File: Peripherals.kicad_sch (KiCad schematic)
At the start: 32 parts, among them J1 1X02PICOBLADE, J3 1X02JST_SH, Q5 DMN3023L, U22 SPI_QUAD_FLASH, U4 ACCEL_LIS3DHTR, U5 PAM8301, X1 MicroSD

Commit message: Use kicad footprints for resistors/capacitors
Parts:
- C10, C14, C20: footprint 32blit:C0402K -> Capacitor_SMD:C_0402_1005Metric
- C17, C3: footprint 32blit:C0603 -> Capacitor_SMD:C_0603_1608Metric
- C23: footprint 32blit:0402 -> Capacitor_SMD:C_0402_1005Metric
- C36: footprint 32blit:C0805 -> Capacitor_SMD:C_0805_2012Metric
- R12, R17, R18, R19, R20, R24, R26, R38, R5: footprint 32blit:R0603 -> Resistor_SMD:R_0603_1608Metric

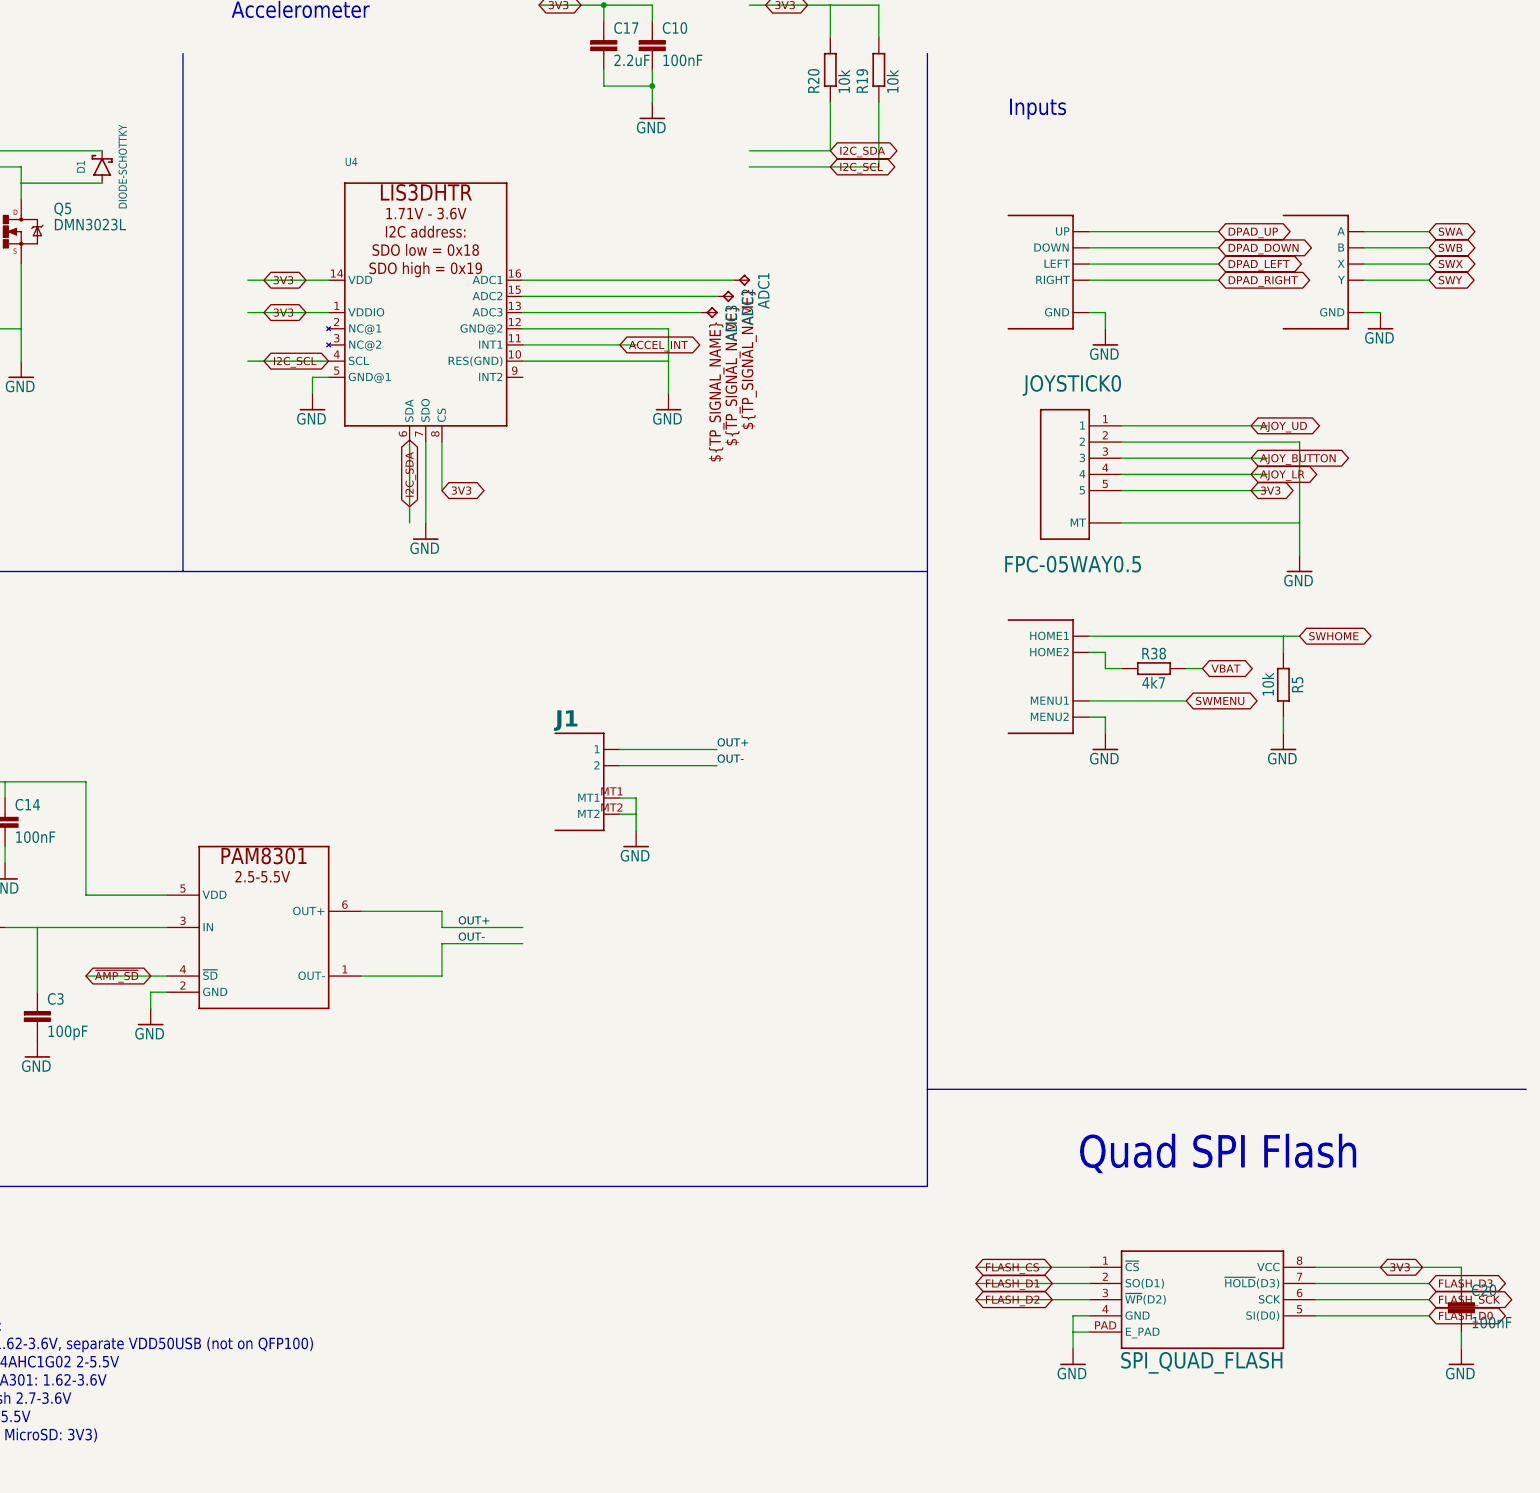
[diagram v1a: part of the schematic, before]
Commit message: More footprint replacements
This involved some adjusting for pad sizes
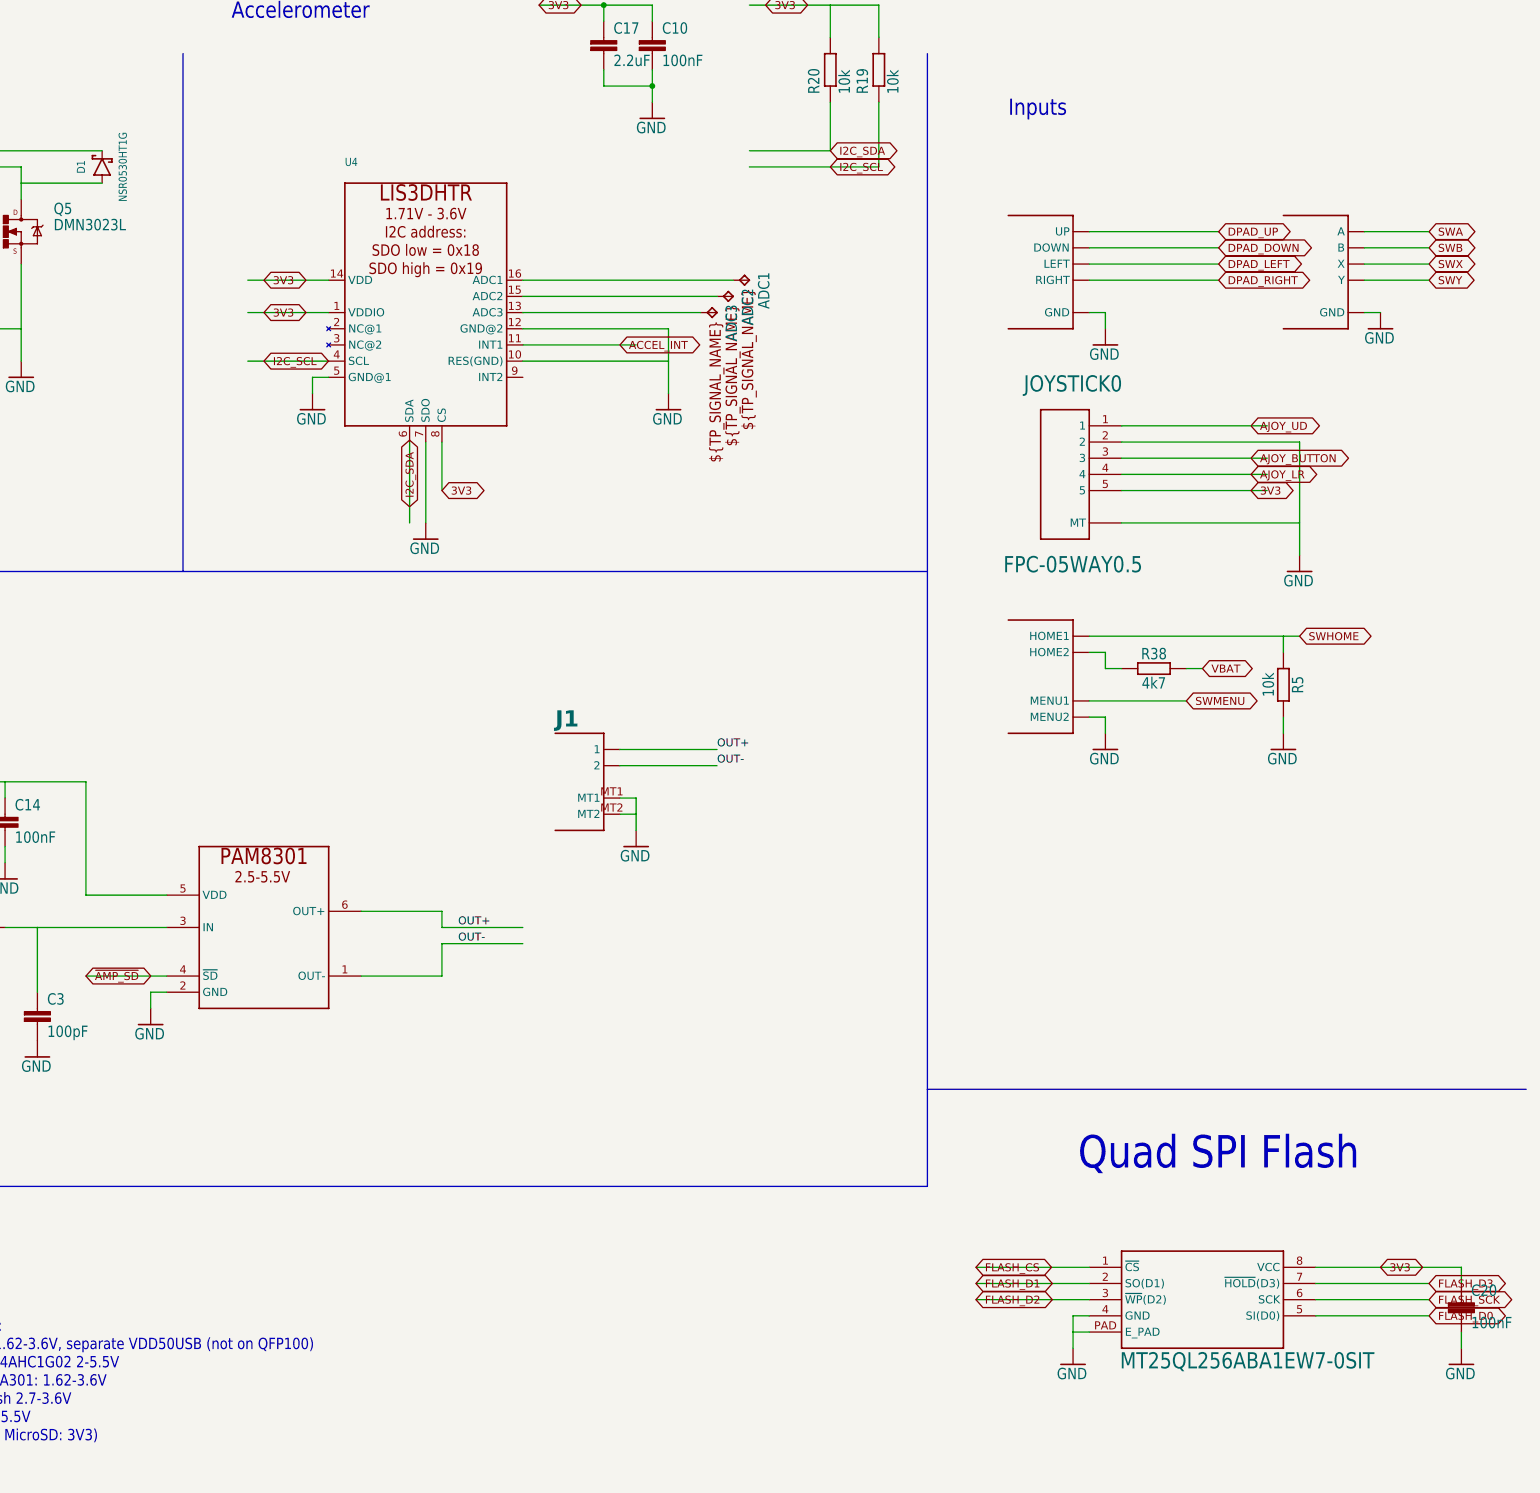
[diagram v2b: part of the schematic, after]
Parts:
- D1: value DIODE-SCHOTTKY -> NSR0530HT1G
- Q5: footprint 32blit:SOT23 -> Package_TO_SOT_SMD:SOT-23
- U22: value SPI_QUAD_FLASH -> MT25QL256ABA1EW7-0SIT
- U4: footprint 32blit:LGA16_3X3MM -> Package_LGA:LGA-16_3x3mm_P0.5mm_LayoutBorder3x5y
- U5: footprint 32blit:SOT-23-6 -> Package_TO_SOT_SMD:SOT-23-6
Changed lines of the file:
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@@
       (effects (font (size 1.27 1.27)) hide)
     )
-    (property "Footprint" "32blit:LGA16_3X3MM" (at 215.9 86.36 0)
+    (property "Footprint" "Package_LGA:LGA-16_3x3mm_P0.5mm_LayoutBorder3x5y" (at 215.9 86.36 0)
       (effects (font (size 1.27 1.27)) hide)
     )
@@
       (effects (font (size 1.27 1.0795)) (justify bottom))
     )
-    (property "Value" "DIODE-SCHOTTKY" (at 167.64 58.42 0)
+    (property "Value" "NSR0530HT1G" (at 167.64 58.42 0)
       (effects (font (size 1.27 1.0795)) (justify top))
     )
@@
       (effects (font (size 1.778 1.5113)) (justify left bottom))
     )
-    (property "Footprint" "32blit:SOT23" (at 152.4 68.58 0)
+    (property "Footprint" "Package_TO_SOT_SMD:SOT-23" (at 152.4 68.58 0)
       (effects (font (size 1.27 1.27)) hide)
     )
@@
       (effects (font (size 1.27 1.27)) hide)
     )
-    (property "Footprint" "32blit:SOT-23-6" (at 190.5 180.34 0)
+    (property "Footprint" "Package_TO_SOT_SMD:SOT-23-6" (at 190.5 180.34 0)
       (effects (font (size 1.27 1.27)) hide)
     )
@@
       (effects (font (size 2.54 2.159)) (justify left bottom) hide)
     )
-    (property "Value" "SPI_QUAD_FLASH" (at 324.866 244.348 0)
+    (property "Value" "MT25QL256ABA1EW7-0SIT" (at 324.866 244.348 0)
       (effects (font (size 2.54 2.159)) (justify left top))
     )

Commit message: Replace speaker/vibration connector footprints
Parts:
- J1: footprint 32blit:PICOBLADE_1.25MM_2P -> Connector_Molex:Molex_PicoBlade_53261-0271_1x02-1MP_P1.25mm_Horizontal
- J3: footprint 32blit:JST_SH_1.0MM_2P -> Connector_JST:JST_SH_SM02B-SRSS-TB_1x02-1MP_P1.00mm_Horizontal
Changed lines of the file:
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@@
       (effects (font (size 1.27 1.27)) hide)
     )
-    (property "Footprint" "32blit:PICOBLADE_1.25MM_2P" (at 236.22 154.94 0)
+    (property "Footprint" "Connector_Molex:Molex_PicoBlade_53261-0271_1x02-1MP_P1.25mm_Horizontal" (at 236.22 154.94 0)
       (effects (font (size 1.27 1.27)) hide)
     )
@@
       (effects (font (size 1.27 1.27)) hide)
     )
-    (property "Footprint" "32blit:JST_SH_1.0MM_2P" (at 109.22 60.96 0)
-      (effects (font (size 1.27 1.27)) hide)
-    )
+    (property "Footprint" "Connector_JST:JST_SH_SM02B-SRSS-TB_1x02-1MP_P1.00mm_Horizontal" (at 109.22 60.96 0)
+      (effects (font (size 1.27 1.27)) hide)
+    )

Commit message: Remove custom pimoroni frame
Makes the sch a bit hard to work with and recreating it in the .kicad_wks seems difficult
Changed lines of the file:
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@@
-    )
-  )
-  (symbol (lib_id "32blit-eagle-import:DINA3_PIM_L") (at 17.78 281.94 0) (unit 1)
-    (in_bom yes) (on_board yes) (dnp no)
-    (property "Reference" "#FRAME1" (at 17.78 281.94 0)
-      (effects (font (size 1.27 1.27)) hide)
-    )
-    (property "Value" "DINA3_PIM_L" (at 17.78 281.94 0)
-      (effects (font (size 1.27 1.27)) hide)
-    )
-    (property "Footprint" "" (at 17.78 281.94 0)
-      (effects (font (size 1.27 1.27)) hide)
-    )
-    (property "Datasheet" "" (at 17.78 281.94 0)
-      (effects (font (size 1.27 1.27)) hide)
-    )
-    (instances
-      (project "32blit"
-        (path "/5e392b0a-93d8-4fe3-995e-b41db5e69183/693b613c-2623-47be-9523-3f9ea9253e71"
-          (reference "#FRAME1") (unit 1)
-        )
-      )
     )
   )

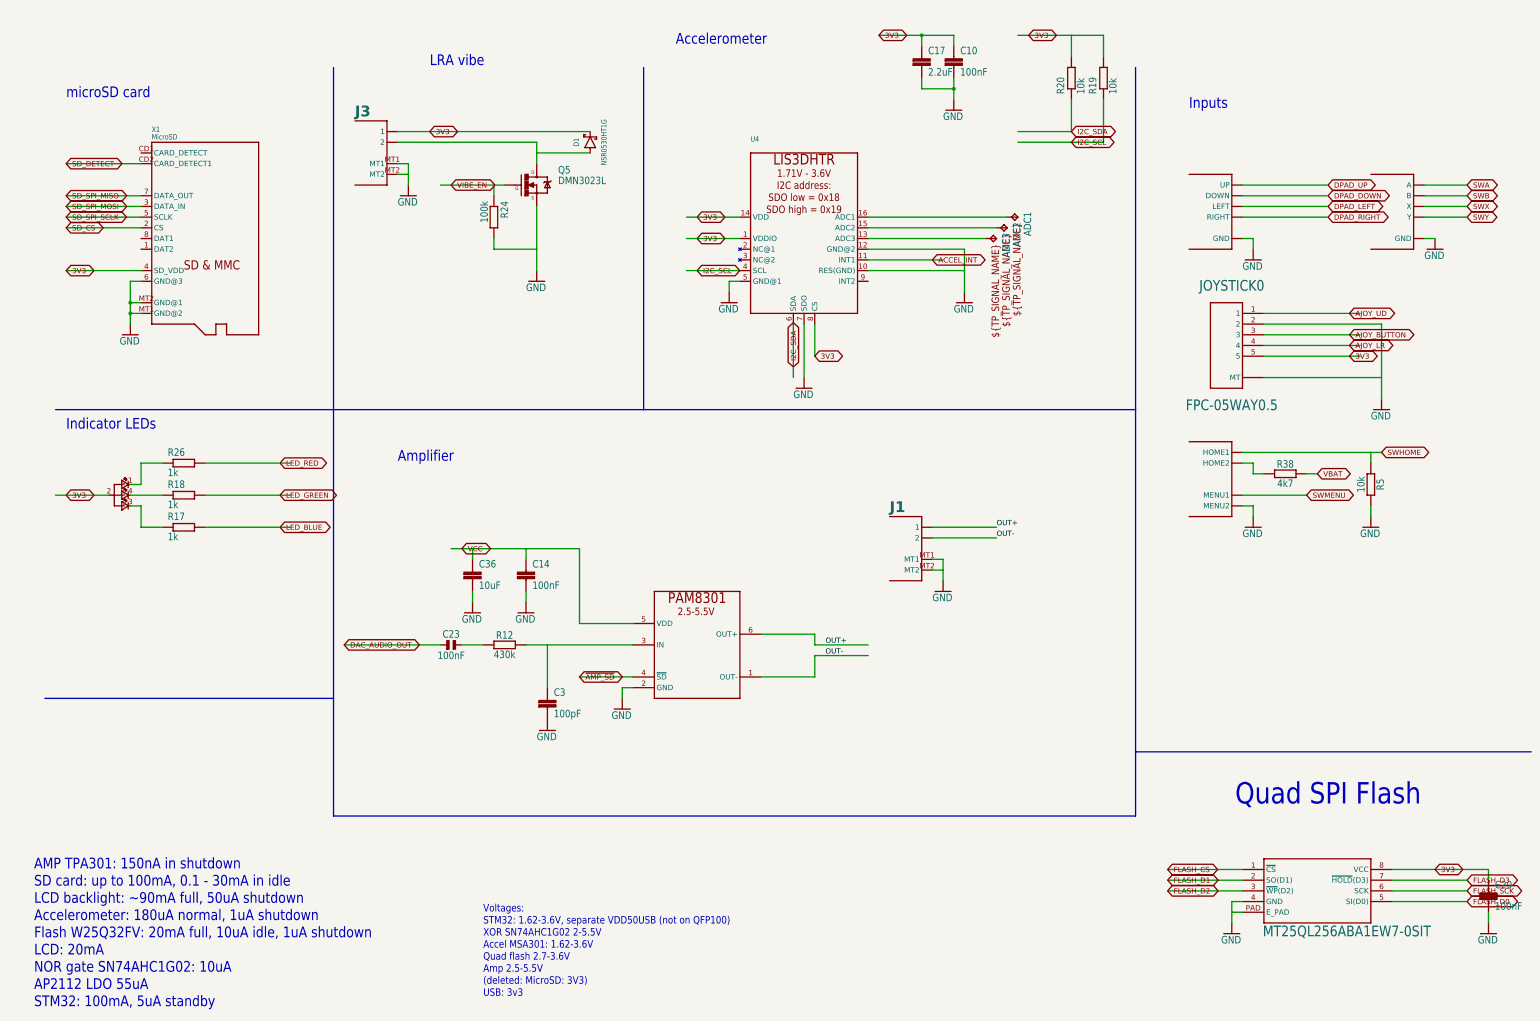
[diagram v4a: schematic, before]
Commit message: Giant schematic rework
Use as many kicad symbols as possiblem, adjust remaining imported symbols to make ERC happy and adjust some footprints for the new symbols
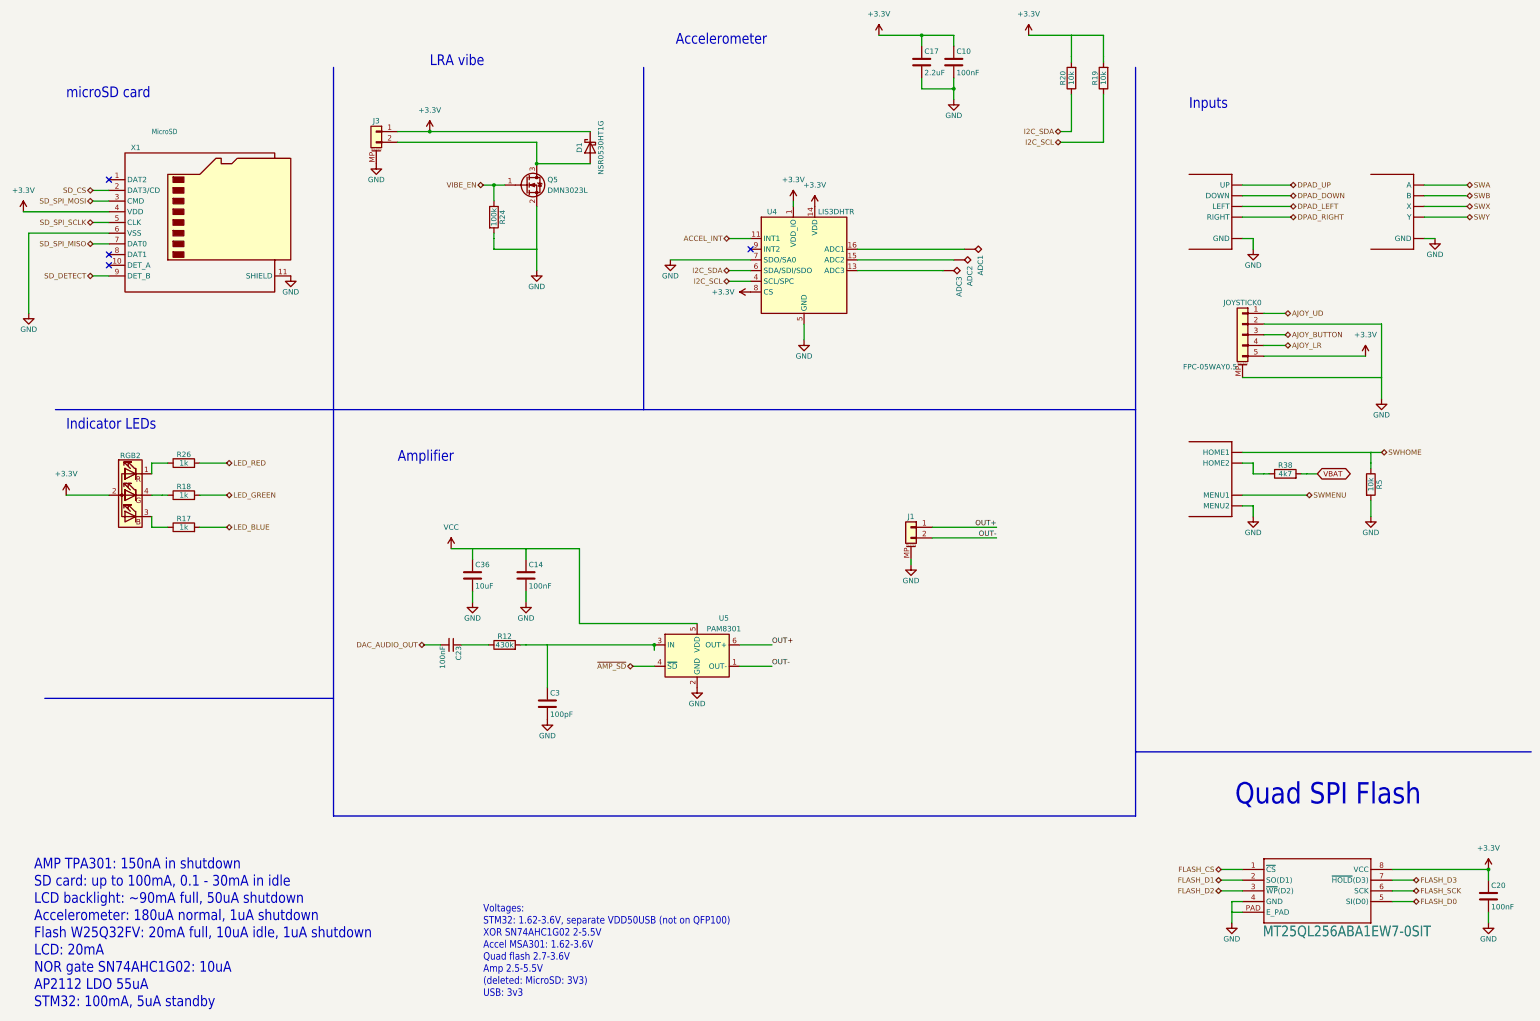
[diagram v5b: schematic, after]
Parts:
- ADC1, ADC2, ADC3: symbol 32blit-eagle-import:TPTP17SQ -> Connector:TestPoint_Alt
- C10, C14: symbol 32blit-eagle-import:C-EUC0402K -> Device:C
- C17, C3: symbol 32blit-eagle-import:C-EUC0603 -> Device:C
- C20: symbol 32blit-eagle-import:rcl_C-EUC0402K -> Device:C
- C23: symbol 32blit-eagle-import:CAPACITOR.0402 -> Device:C_Small
- C36: symbol 32blit-eagle-import:C-EUC0805 -> Device:C
- D1: symbol 32blit-eagle-import:DIODE-SCHOTTKY -> Device:D_Schottky
- J1: symbol 32blit-eagle-import:1X02PICOBLADE -> Connector_Generic_MountingPin:Conn_01x02_MountingPin
- J3: symbol 32blit-eagle-import:1X02JST_SH -> Connector_Generic_MountingPin:Conn_01x02_MountingPin
- JOYSTICK0: symbol 32blit-eagle-import:FPC-05WAY0.5 -> Connector_Generic_MountingPin:Conn_01x05_MountingPin
- Q5: symbol 32blit-eagle-import:MOSFET-NCHANNEL -> Device:Q_NMOS_GSD
- R12, R17, R18, R19, R20, R24, R26, R38, R5: symbol 32blit-eagle-import:R-EU_R0603 -> Device:R
- RGB2: symbol 32blit-eagle-import:LED_RGB_4P6028_REVERSE -> Device:LED_RABG
- U4: value ACCEL_LIS3DHTR -> LIS3DHTR; symbol 32blit-eagle-import:ACCEL_LIS3DHTR -> Sensor_Motion:LIS3DH
- U5: symbol 32blit-eagle-import:PAM8301 -> Amplifier_Audio:PAM8301
- X1: symbol 32blit-eagle-import:MICROSD -> Connector:Micro_SD_Card_Det2
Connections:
- net GND: now also J1.MP (MountPin), J3.MP (MountPin), JOYSTICK0.MP (MountPin), X1.11 (SHIELD); no longer J1.MT1, J1.MT2, J3.MT1, J3.MT2, JOYSTICK0.MT1 (MT), JOYSTICK0.MT2 (MT), X1.MT1 (GND@2), X1.MT2 (GND@1)
- net SD_DETECT: now also X1.9 (DET_B); no longer X1.CD2 (CARD_DETECT1)
- net at U4.13 (ADC3): now also ADC3.1; no longer ADC3.TP
- net at U4.15 (ADC2): now also ADC2.1; no longer ADC2.TP
- net at U4.16 (ADC1): now also ADC1.1; no longer ADC1.TP
- net at J3.2 (Pin_2), Q5.3 (D): now also D1.2 (A); no longer D1.A
- net 3V3 renamed +3.3V
- net +3.3V: now also D1.1 (K); no longer D1.C
- no-connect marks 0 -> 4
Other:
- moved on the sheet: JOYSTICK0
